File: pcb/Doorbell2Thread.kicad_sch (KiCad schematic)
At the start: 11 parts, among them J1 Klingel, Q1 2N7002, Q2 2N7002, SW1 TS-1088, SW2 TS-1088, U1 ESP32-H2-Zero, U2 LMS78_03-0.5R

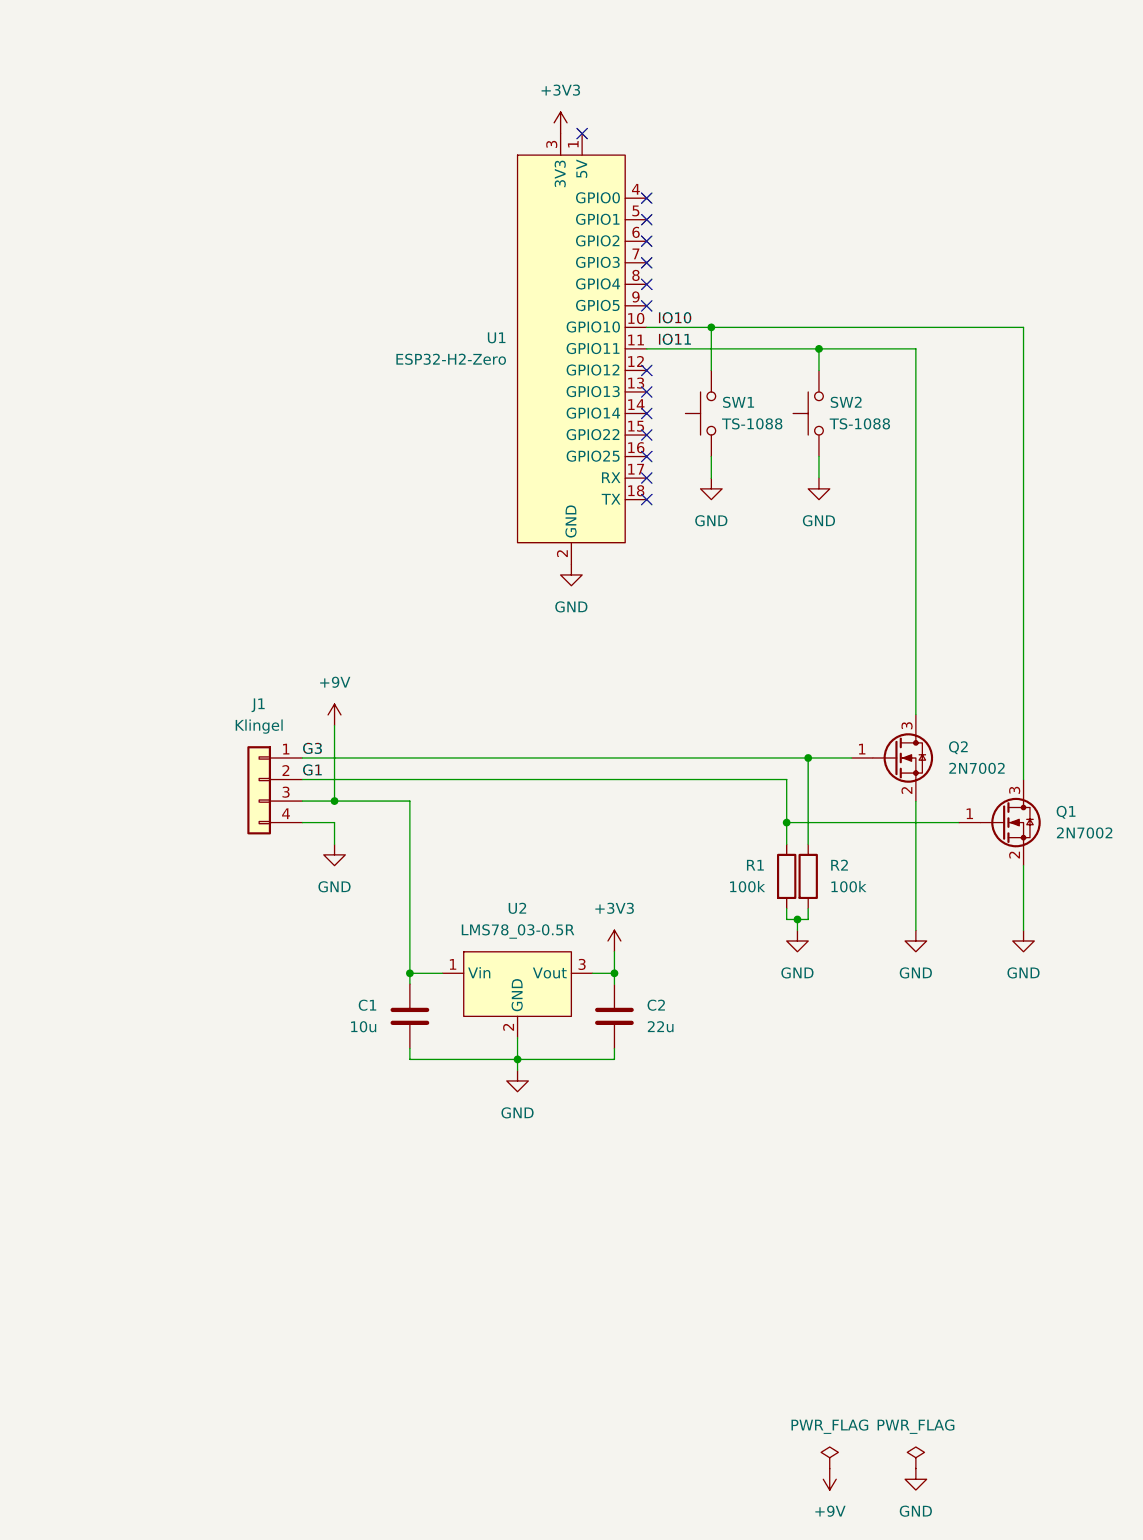
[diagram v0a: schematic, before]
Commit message: fix: add protection circuitry
The doorbell was killing the mosfets on the board so some protection was needed

feat: replaced the expensive LME78
This caused a major redesign of the whole board

fix: update to KiCad 10
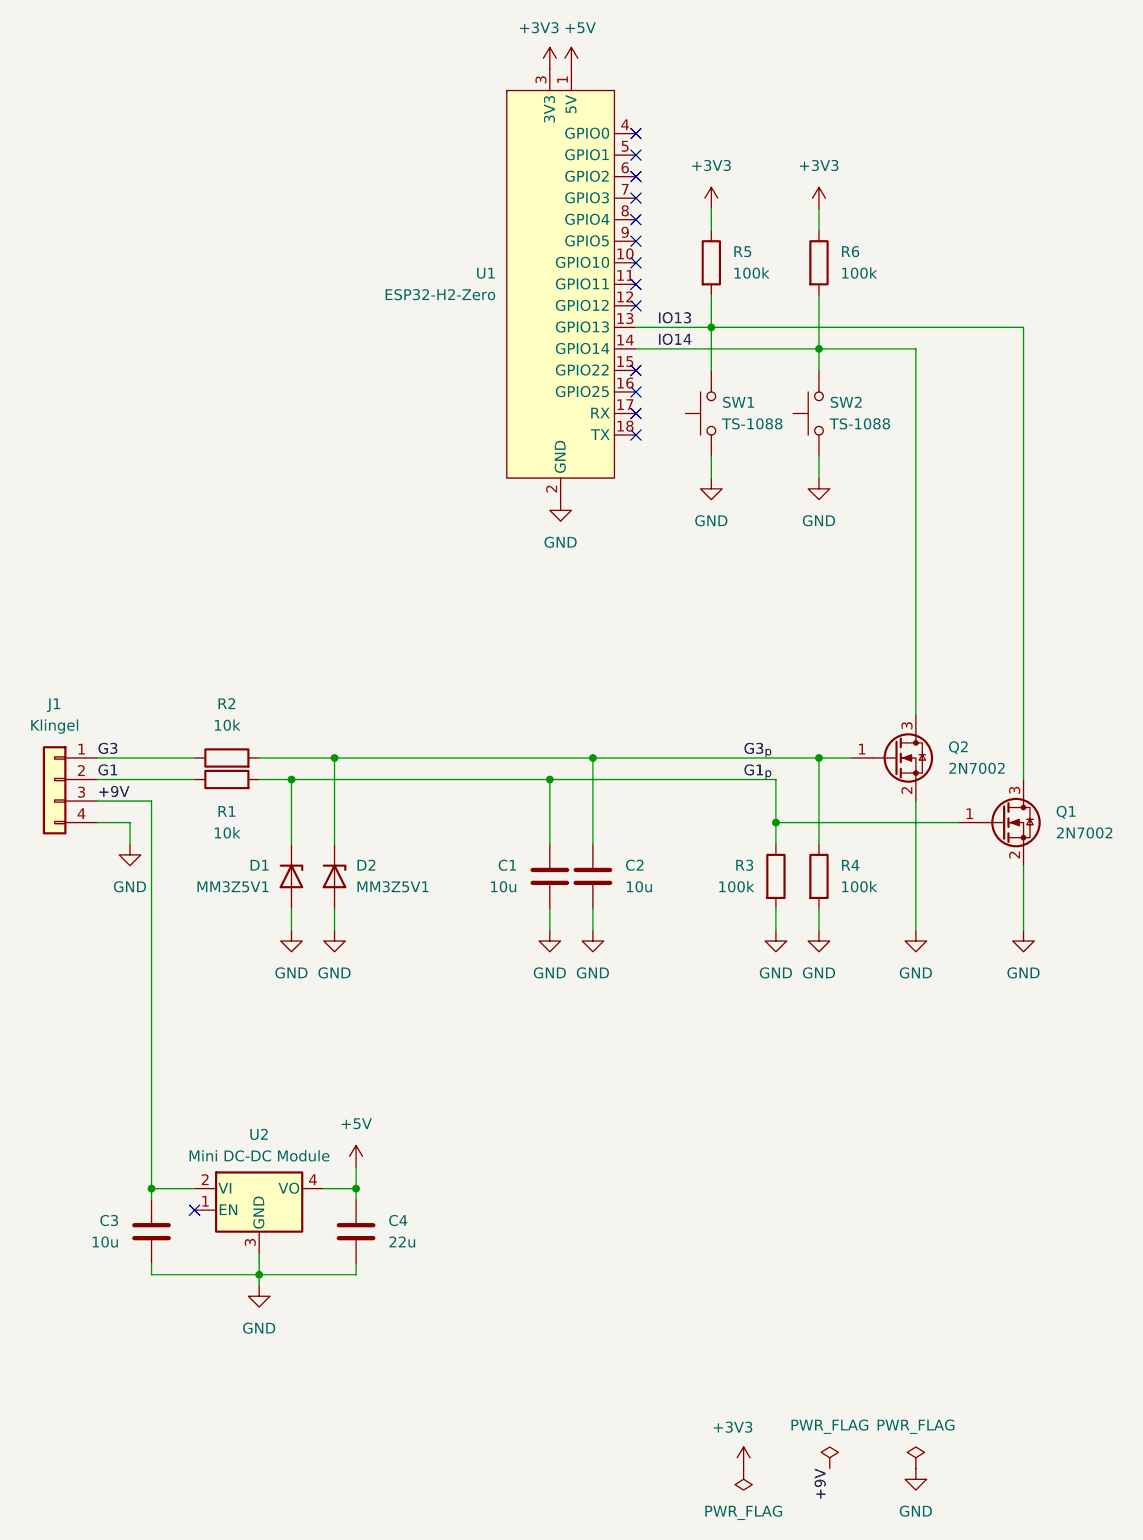
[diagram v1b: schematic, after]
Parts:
- removed U2: LMS78_03-0.5R, My_Footprints:LME78_1.0-Series, symbol My_Symbols:LME78
- added C1, C2: 10u, Capacitor_SMD:C_0603_1608Metric, symbol Device:C
- added D1, D2: MM3Z5V1, Diode_SMD:D_SOD-323, symbol Diode:MM3Zxx
- added R1, R2: 10k, Resistor_SMD:R_0402_1005Metric, symbol Device:R
- added R5, R6: 100k, Resistor_SMD:R_0402_1005Metric, symbol Device:R
- added U2: Mini DC-DC Module, My_Footprints:Mini DC-DC Module, symbol My_Symbols:Mini DC-DC Module
- R3: renamed from R1; footprint Resistor_SMD:R_0603_1608Metric -> Resistor_SMD:R_0402_1005Metric; LCSC C25803 -> C25741
- R4: renamed from R2; footprint Resistor_SMD:R_0603_1608Metric -> Resistor_SMD:R_0402_1005Metric; LCSC C25803 -> C25741
- renumbered C1 to C3, C2 to C4, Q2 to Q1, Q1 to Q2
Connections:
- net +3V3: now also R5.1, R6.1; no longer C4.1
- net +9V: now also U2.2 (VI)
- net G1: now also R1.1; no longer Q2.1 (G), R3.1
- net G3: now also R2.1; no longer Q1.1 (G), R4.1
- net GND: now also C1.2, C2.2, D1.2 (A), D2.2 (A), U2.3 (GND)
- net +5V: now reaches U1.1 (5V)
- net +5V: now also C4.1, U2.4 (VO)
- net IO13: now reaches U1.13 (GPIO13)
- net IO13: now also Q1.3 (D), SW1.2, R5.2
- net IO14: now reaches U1.14 (GPIO14)
- net IO14: now also Q2.3 (D), SW2.2, R6.2
- removed net IO10: Q2.3 (D), SW1.2, U1.10 (GPIO10)
- removed net IO11: Q1.3 (D), SW2.2, U1.11 (GPIO11)
- new net G1_{p}: C1.1, D1.1 (K), Q1.1 (G), R1.2, R3.1
- new net G3_{p}: C2.1, D2.1 (K), Q2.1 (G), R2.2, R4.1
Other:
- moved on the sheet: C3, C4, J1, Q1, Q2, R3, R4, U1
